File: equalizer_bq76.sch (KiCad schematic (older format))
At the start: 10 parts

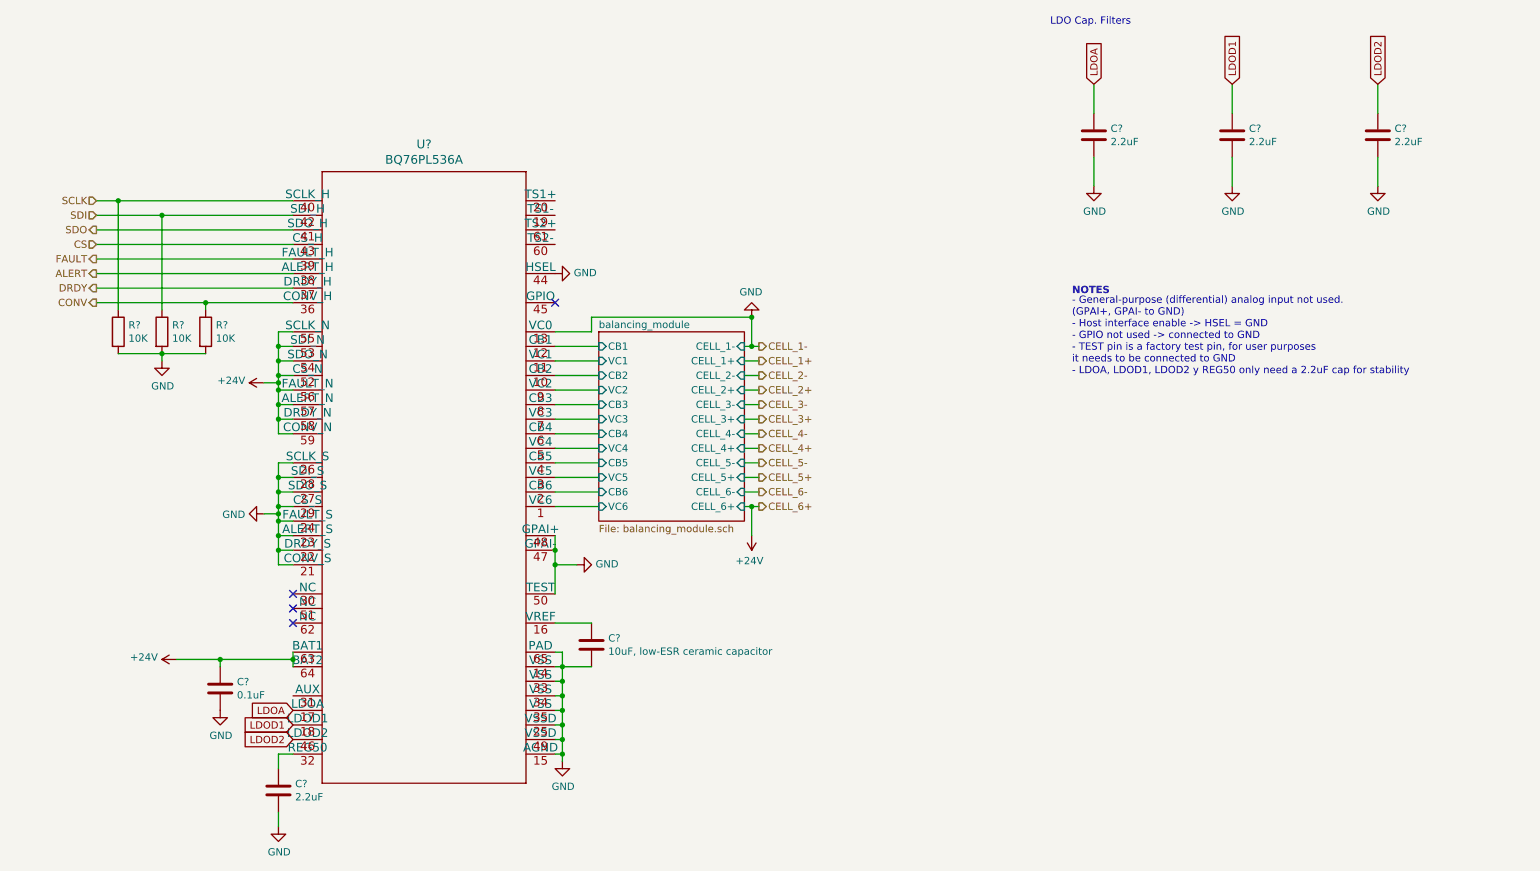
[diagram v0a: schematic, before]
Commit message: mmoya/bq76pl536a Adds current sensor and IO for hierarchical sheet
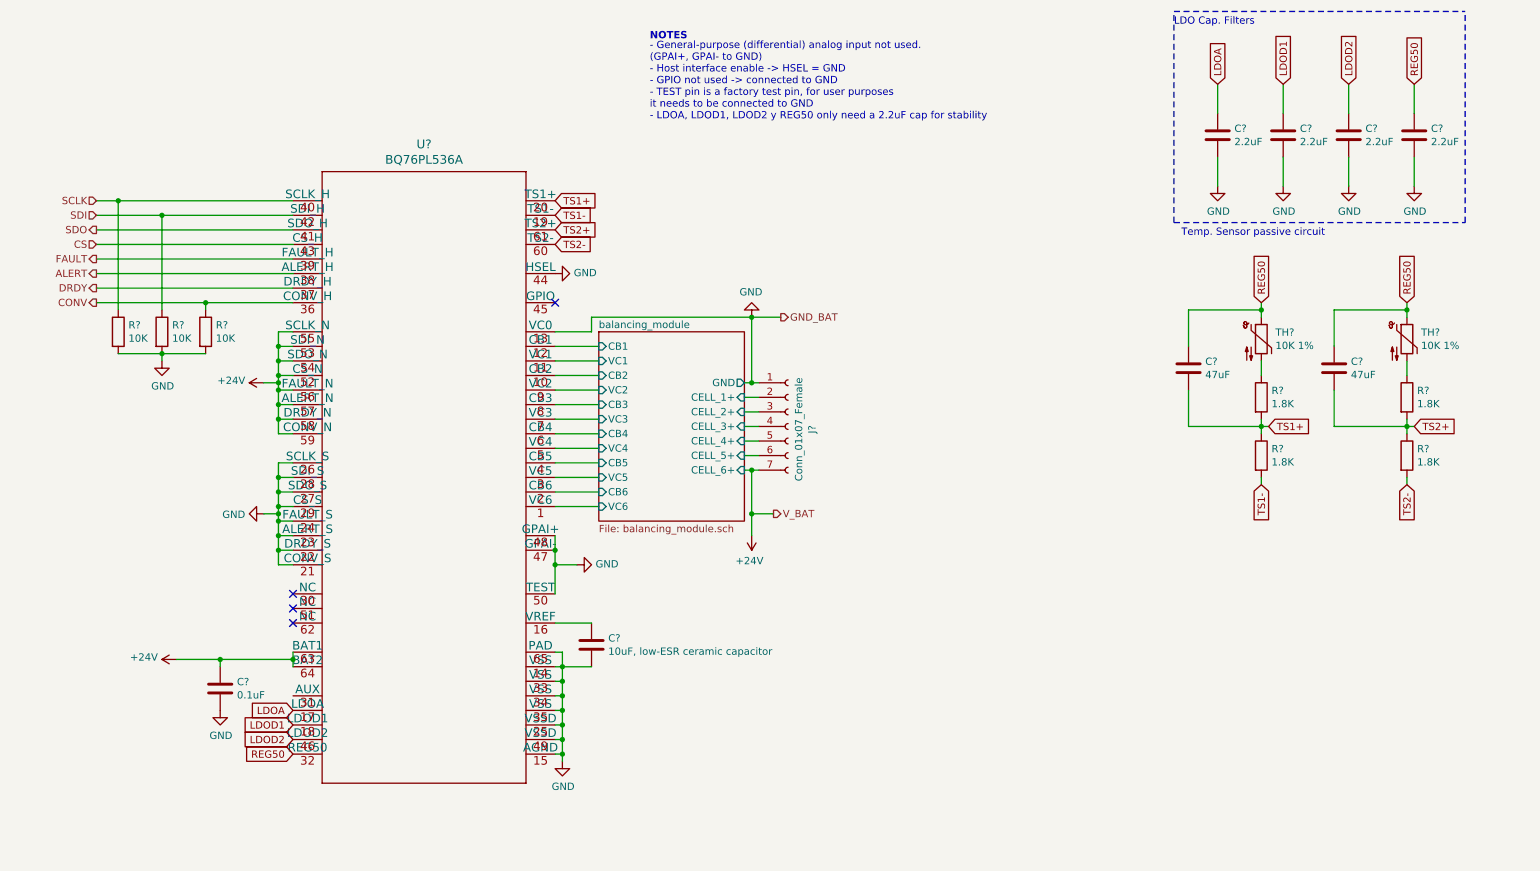
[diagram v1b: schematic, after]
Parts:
- removed C?: 2.2uF, Capacitor_SMD:C_0805_2012Metric_Pad1.18x1.45mm_HandSolder, symbol Device:C
- added C?: 2.2uF, Capacitor_SMD:C_0805_2012Metric_Pad1.18x1.45mm_HandSolder, symbol Device:C
- added C? (x2): 47uF, Capacitor_SMD:C_0805_2012Metric_Pad1.18x1.45mm_HandSolder, symbol Device:C
- added J?: Conn_01x07_Female, symbol Connector:Conn_01x07_Female
- added R? (x4): 1.8K, Resistor_SMD:R_0805_2012Metric_Pad1.20x1.40mm_HandSolder, symbol Device:R
- added TH? (x2): 10K 1%, Connector_JST:JST_XH_S2B-XH-A_1x02_P2.50mm_Horizontal, symbol Device:Thermistor_NTC
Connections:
- net +24V: now also J?.7 (Pin_7)
- net GND: now also C?.2, J?.1 (Pin_1)
- net TS1-: now reaches U?.19 (TS1-)
- net TS1-: now also R?.2
- net TS1+: now reaches U?.20 (TS1+)
- net TS1+: now also C?.2, R?.1, R?.2
- net REG50: now reaches U?.32 (REG50)
- net REG50: now also C?.1, C?.1, C?.1, TH?.1, TH?.1
- net TS2-: now reaches U?.60 (TS2-)
- net TS2-: now also R?.2
- net TS2+: now reaches U?.61 (TS2+)
- net TS2+: now also C?.2, R?.1, R?.2
- new net: R?.1, TH?.2 (x2)
- new net balancing_module/CELL_1+: J?.2 (Pin_2)
- new net balancing_module/CELL_2+: J?.3 (Pin_3)
- new net balancing_module/CELL_3+: J?.4 (Pin_4)
- new net balancing_module/CELL_4+: J?.5 (Pin_5)
- new net balancing_module/CELL_5+: J?.6 (Pin_6)
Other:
- note added: "Temp. Sensor passive circuit"
- moved on the sheet: C?

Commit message: Adds missing footprints for conns
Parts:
- J2: renamed from J?; footprint (none) -> Connector_JST:JST_XH_S7B-XH-A_1x07_P2.50mm_Horizontal
- gave numbers to parts that had none: 18
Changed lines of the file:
@@
 $EndDescr
 $Comp
-L power:GND #PWR?
+L power:GND #PWR0116
 U 1 1 5FE79F0F
 P 5000 5700
-F 0 "#PWR?" H 5000 5450 50  0001 C CNN
+F 0 "#PWR0116" H 5000 5450 50  0001 C CNN
 F 1 "GND" H 5005 5527 50  0000 C CNN
 F 2 "" H 5000 5700 50  0001 C CNN
@@
 	5000 5650 5000 5700
 $Comp
-L Device:C C?
+L Device:C C18
 U 1 1 5FE7B3CE
 P 5200 4900
-F 0 "C?" H 5315 4946 50  0000 L CNN
+F 0 "C18" H 5315 4946 50  0000 L CNN
 F 1 "10uF, low-ESR ceramic capacitor" H 5315 4855 50  0000 L CNN
 F 2 "Capacitor_SMD:C_0805_2012Metric_Pad1.18x1.45mm_HandSolder" H 5238 4750 50  0001 C CNN
@@
 	5200 2650 6300 2650
 $Comp
-L power:+24V #PWR?
+L power:+24V #PWR0117
 U 1 1 5FF5699F
 P 6300 4150
-F 0 "#PWR?" H 6300 4000 50  0001 C CNN
+F 0 "#PWR0117" H 6300 4000 50  0001 C CNN
 F 1 "+24V" H 6315 4323 50  0000 C CNN
 F 2 "" H 6300 4150 50  0001 C CNN
@@
 	3050 2850 3050 2950
 $Comp
-L power:+24V #PWR?
+L power:+24V #PWR0118
 U 1 1 5FF5DCD5
 P 2950 3100
-F 0 "#PWR?" H 2950 2950 50  0001 C CNN
+F 0 "#PWR0118" H 2950 2950 50  0001 C CNN
 F 1 "+24V" V 2965 3228 50  0000 L CNN
 F 2 "" H 2950 3100 50  0001 C CNN
@@
 	3150 5050 3150 5000
 $Comp
-L power:+24V #PWR?
+L power:+24V #PWR0119
 U 1 1 5FF6167E
 P 2350 5000
-F 0 "#PWR?" H 2350 4850 50  0001 C CNN
+F 0 "#PWR0119" H 2350 4850 50  0001 C CNN
 F 1 "+24V" V 2365 5128 50  0000 L CNN
 F 2 "" H 2350 5000 50  0001 C CNN
@@
 	3050 3750 3050 3850
 $Comp
-L power:GND #PWR?
+L power:GND #PWR0120
 U 1 1 5FF6D984
 P 2950 4000
-F 0 "#PWR?" H 2950 3750 50  0001 C CNN
+F 0 "#PWR0120" H 2950 3750 50  0001 C CNN
 F 1 "GND" V 2955 3872 50  0000 R CNN
 F 2 "" H 2950 4000 50  0001 C CNN
@@
 LDOD2
 $Comp
-L Device:C C?
+L Device:C C21
 U 1 1 5FF753CC
 P 9950 1400
-F 0 "C?" H 10065 1446 50  0000 L CNN
+F 0 "C21" H 10065 1446 50  0000 L CNN
 F 1 "2.2uF" H 10065 1355 50  0000 L CNN
 F 2 "Capacitor_SMD:C_0805_2012Metric_Pad1.18x1.45mm_HandSolder" H 9988 1250 50  0001 C CNN
@@
 $EndComp
 $Comp
-L power:GND #PWR?
+L power:GND #PWR0121
 U 1 1 5FF77895
 P 9950 1750
-F 0 "#PWR?" H 9950 1500 50  0001 C CNN
+F 0 "#PWR0121" H 9950 1500 50  0001 C CNN
 F 1 "GND" H 9955 1577 50  0000 C CNN
 F 2 "" H 9950 1750 50  0001 C CNN
@@
 LDOD2
 $Comp
-L Device:C C?
+L Device:C C23
 U 1 1 5FF9A6DD
 P 10400 1400
-F 0 "C?" H 10515 1446 50  0000 L CNN
+F 0 "C23" H 10515 1446 50  0000 L CNN
 F 1 "2.2uF" H 10515 1355 50  0000 L CNN
 F 2 "Capacitor_SMD:C_0805_2012Metric_Pad1.18x1.45mm_HandSolder" H 10438 1250 50  0001 C CNN
@@
 $EndComp
 $Comp
-L power:GND #PWR?
+L power:GND #PWR0122
 U 1 1 5FF9A6E5
 P 10400 1750
-F 0 "#PWR?" H 10400 1500 50  0001 C CNN
+F 0 "#PWR0122" H 10400 1500 50  0001 C CNN
 F 1 "GND" H 10405 1577 50  0000 C CNN
 F 2 "" H 10400 1750 50  0001 C CNN
@@
 $EndComp
 $Comp
-L Device:C C?
+L Device:C C20
 U 1 1 5FFA673C
 P 9500 1400
-F 0 "C?" H 9615 1446 50  0000 L CNN
+F 0 "C20" H 9615 1446 50  0000 L CNN
 F 1 "2.2uF" H 9615 1355 50  0000 L CNN
 F 2 "Capacitor_SMD:C_0805_2012Metric_Pad1.18x1.45mm_HandSolder" H 9538 1250 50  0001 C CNN
@@
 $EndComp
 $Comp
-L power:GND #PWR?
+L power:GND #PWR0123
 U 1 1 5FFA6744
 P 9500 1750
-F 0 "#PWR?" H 9500 1500 50  0001 C CNN
+F 0 "#PWR0123" H 9500 1500 50  0001 C CNN
 F 1 "GND" H 9505 1577 50  0000 C CNN
 F 2 "" H 9500 1750 50  0001 C CNN
@@
 $EndComp
 $Comp
-L Device:C C?
+L Device:C C17
 U 1 1 5FFAD9BF
 P 2650 5200
-F 0 "C?" H 2765 5246 50  0000 L CNN
+F 0 "C17" H 2765 5246 50  0000 L CNN
 F 1 "0.1uF" H 2765 5155 50  0000 L CNN
 F 2 "Capacitor_SMD:C_0805_2012Metric_Pad1.18x1.45mm_HandSolder" H 2688 5050 50  0001 C CNN
@@
 	2650 5000 3150 5000
 $Comp
-L power:GND #PWR?
+L power:GND #PWR0124
 U 1 1 5FFB4473
 P 2650 5350
-F 0 "#PWR?" H 2650 5100 50  0001 C CNN
+F 0 "#PWR0124" H 2650 5100 50  0001 C CNN
 F 1 "GND" H 2655 5177 50  0000 C CNN
 F 2 "" H 2650 5350 50  0001 C CNN
@@
 $EndComp
 $Comp
-L power:GND #PWR?
+L power:GND #PWR0125
 U 1 1 5FFB8D43
 P 4950 2350
-F 0 "#PWR?" H 4950 2100 50  0001 C CNN
+F 0 "#PWR0125" H 4950 2100 50  0001 C CNN
 F 1 "GND" V 4955 2222 50  0000 R CNN
 F 2 "" H 4950 2350 50  0001 C CNN
@@
 LDO Cap. Filters
 $Comp
-L power:GND #PWR?
+L power:GND #PWR0126
 U 1 1 6001D855
 P 5100 4350
-F 0 "#PWR?" H 5100 4100 50  0001 C CNN
+F 0 "#PWR0126" H 5100 4100 50  0001 C CNN
 F 1 "GND" V 5105 4222 50  0000 R CNN
 F 2 "" H 5100 4350 50  0001 C CNN
@@
 LDOA
 $Comp
-L Device:R R?
+L Device:R R4
 U 1 1 6003EECE
 P 1950 2750
-F 0 "R?" H 2020 2796 50  0000 L CNN
+F 0 "R4" H 2020 2796 50  0000 L CNN
 F 1 "10K" H 2020 2705 50  0000 L CNN
 F 2 "Resistor_SMD:R_0805_2012Metric_Pad1.20x1.40mm_HandSolder" V 1880 2750 50  0001 C CNN
@@
 $EndComp
 $Comp
-L Device:R R?
+L Device:R R5
 U 1 1 6003F38A
 P 2250 2750
-F 0 "R?" H 2320 2796 50  0000 L CNN
+F 0 "R5" H 2320 2796 50  0000 L CNN
 F 1 "10K" H 2320 2705 50  0000 L CNN
 F 2 "Resistor_SMD:R_0805_2012Metric_Pad1.20x1.40mm_HandSolder" V 2180 2750 50  0001 C CNN
@@
 $EndComp
 $Comp
-L Device:R R?
+L Device:R R6
 U 1 1 6003F59D
 P 2550 2750
-F 0 "R?" H 2620 2796 50  0000 L CNN
+F 0 "R6" H 2620 2796 50  0000 L CNN
 F 1 "10K" H 2620 2705 50  0000 L CNN
 F 2 "Resistor_SMD:R_0805_2012Metric_Pad1.20x1.40mm_HandSolder" V 2480 2750 50  0001 C CNN
@@
 	2250 2900 2550 2900
 $Comp
-L power:GND #PWR?
+L power:GND #PWR0127
 U 1 1 6005D886
 P 2250 2950
-F 0 "#PWR?" H 2250 2700 50  0001 C CNN
+F 0 "#PWR0127" H 2250 2700 50  0001 C CNN
 F 1 "GND" H 2255 2777 50  0000 C CNN
 F 2 "" H 2250 2950 50  0001 C CNN
@@
 Connection ~ 2550 2550
 $Comp
-L power:GND #PWR?
+L power:GND #PWR0128
 U 1 1 5FEA2AD8
 P 6300 2650
-F 0 "#PWR?" H 6300 2400 50  0001 C CNN
+F 0 "#PWR0128" H 6300 2400 50  0001 C CNN
 F 1 "GND" H 6305 2477 50  0000 C CNN
 F 2 "" H 6300 2650 50  0001 C CNN
@@
 $EndComp
 $Comp
-L Device:R R?
+L Device:R R9
 U 1 1 5FE93DA5
 P 10800 3200
-F 0 "R?" H 10870 3246 50  0000 L CNN
+F 0 "R9" H 10870 3246 50  0000 L CNN
 F 1 "1.8K" H 10870 3155 50  0000 L CNN
 F 2 "Resistor_SMD:R_0805_2012Metric_Pad1.20x1.40mm_HandSolder" V 10730 3200 50  0001 C CNN
@@
 $EndComp
 $Comp
-L Device:R R?
+L Device:R R10
 U 1 1 5FE942F6
 P 10800 3600
-F 0 "R?" H 10870 3646 50  0000 L CNN
+F 0 "R10" H 10870 3646 50  0000 L CNN
 F 1 "1.8K" H 10870 3555 50  0000 L CNN
 F 2 "Resistor_SMD:R_0805_2012Metric_Pad1.20x1.40mm_HandSolder" V 10730 3600 50  0001 C CNN
@@
 Temp. Sensor passive circuit
 $Comp
-L Device:Thermistor_NTC TH?
+L Device:Thermistor_NTC TH2
 U 1 1 5FEB224A
 P 10800 2800
-F 0 "TH?" H 10897 2846 50  0000 L CNN
+F 0 "TH2" H 10897 2846 50  0000 L CNN
 F 1 "10K 1%" H 10897 2755 50  0000 L CNN
 F 2 "Connector_JST:JST_XH_S2B-XH-A_1x02_P2.50mm_Horizontal" H 10800 2850 50  0001 C CNN
@@
 Connection ~ 4950 4250
 $Comp
-L Battery_Management:BQ76PL536A U?
+L Battery_Management:BQ76PL536A U2
 U 1 1 5FE7709D
 P 4050 3750
-F 0 "U?" H 4050 6038 60  0000 C CNN
+F 0 "U2" H 4050 6038 60  0000 C CNN
 F 1 "BQ76PL536A" H 4050 5932 60  0000 C CNN
 F 2 "Package_QFP:HTQFP-64-1EP_10x10mm_P0.5mm_EP8x8mm" H 4050 3690 60  0001 C CNN
@@
 REG50
 $Comp
-L Device:C C?
+L Device:C C24
 U 1 1 5FECF8E1
 P 10850 1400
-F 0 "C?" H 10965 1446 50  0000 L CNN
+F 0 "C24" H 10965 1446 50  0000 L CNN
 F 1 "2.2uF" H 10965 1355 50  0000 L CNN
 F 2 "Capacitor_SMD:C_0805_2012Metric_Pad1.18x1.45mm_HandSolder" H 10888 1250 50  0001 C CNN
@@
 $EndComp
 $Comp
-L power:GND #PWR?
+L power:GND #PWR0129
 U 1 1 5FECF8E7
 P 10850 1750
-F 0 "#PWR?" H 10850 1500 50  0001 C CNN
+F 0 "#PWR0129" H 10850 1500 50  0001 C CNN
 F 1 "GND" H 10855 1577 50  0000 C CNN
 F 2 "" H 10850 1750 50  0001 C CNN
@@
 REG50
 $Comp
-L Device:C C?
+L Device:C C22
 U 1 1 5FEFD46C
 P 10300 3000
-F 0 "C?" H 10415 3046 50  0000 L CNN
+F 0 "C22" H 10415 3046 50  0000 L CNN
 F 1 "47uF" H 10415 2955 50  0000 L CNN
 F 2 "Capacitor_SMD:C_0805_2012Metric_Pad1.18x1.45mm_HandSolder" H 10338 2850 50  0001 C CNN
@@
 	10800 3750 10800 3800
 $Comp
-L Device:R R?
+L Device:R R7
 U 1 1 5FF2491E
 P 9800 3200
-F 0 "R?" H 9870 3246 50  0000 L CNN
+F 0 "R7" H 9870 3246 50  0000 L CNN
 F 1 "1.8K" H 9870 3155 50  0000 L CNN
 F 2 "Resistor_SMD:R_0805_2012Metric_Pad1.20x1.40mm_HandSolder" V 9730 3200 50  0001 C CNN
@@
 $EndComp
 $Comp
-L Device:R R?
+L Device:R R8
 U 1 1 5FF24924
 P 9800 3600
-F 0 "R?" H 9870 3646 50  0000 L CNN
+F 0 "R8" H 9870 3646 50  0000 L CNN
 F 1 "1.8K" H 9870 3555 50  0000 L CNN
 F 2 "Resistor_SMD:R_0805_2012Metric_Pad1.20x1.40mm_HandSolder" V 9730 3600 50  0001 C CNN
@@
 	9800 3350 9800 3400
 $Comp
-L Device:Thermistor_NTC TH?
+L Device:Thermistor_NTC TH1
 U 1 1 5FF2492B
 P 9800 2800
-F 0 "TH?" H 9897 2846 50  0000 L CNN
+F 0 "TH1" H 9897 2846 50  0000 L CNN
 F 1 "10K 1%" H 9897 2755 50  0000 L CNN
 F 2 "Connector_JST:JST_XH_S2B-XH-A_1x02_P2.50mm_Horizontal" H 9800 2850 50  0001 C CNN
@@
 REG50
 $Comp
-L Device:C C?
+L Device:C C19
 U 1 1 5FF24933
 P 9300 3000
-F 0 "C?" H 9415 3046 50  0000 L CNN
+F 0 "C19" H 9415 3046 50  0000 L CNN
 F 1 "47uF" H 9415 2955 50  0000 L CNN
 F 2 "Capacitor_SMD:C_0805_2012Metric_Pad1.18x1.45mm_HandSolder" H 9338 2850 50  0001 C CNN
@@
 Connection ~ 6300 2650
 $Comp
-L Connector:Conn_01x07_Female J?
+L Connector:Conn_01x07_Female J2
 U 1 1 5FF8226F
 P 6550 3400
-F 0 "J?" V 6715 3380 50  0000 C CNN
+F 0 "J2" V 6715 3380 50  0000 C CNN
 F 1 "Conn_01x07_Female" V 6624 3380 50  0000 C CNN
-F 2 "" H 6550 3400 50  0001 C CNN
+F 2 "Connector_JST:JST_XH_S7B-XH-A_1x07_P2.50mm_Horizontal" H 6550 3400 50  0001 C CNN
 F 3 "~" H 6550 3400 50  0001 C CNN
 	1    6550 3400

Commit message: Changes overlapping names of pins between bq76 and ina226
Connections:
- net ALERT renamed ALERT_BQ76
- net CONV renamed CONV_BQ76
- net DRDY renamed DRDY_BQ76
- net FAULT renamed FAULT_BQ76
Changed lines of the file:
@@
 $Descr A4 11693 8268
 encoding utf-8
-Sheet 3 5
+Sheet 2 5
 Title ""
 Date ""
@@
 	3150 2150 1800 2150
 Text HLabel 1800 2250 0    50   Output ~ 0
-FAULT
+FAULT_BQ76
 Wire Wire Line
 	1800 2250 3150 2250
 Text HLabel 1800 2350 0    50   Output ~ 0
-ALERT
+ALERT_BQ76
 Wire Wire Line
 	1800 2350 3150 2350
 Text HLabel 1800 2450 0    50   Output ~ 0
-DRDY
+DRDY_BQ76
 Wire Wire Line
 	3150 2450 1800 2450
 Text HLabel 1800 2550 0    50   Output ~ 0
-CONV
+CONV_BQ76
 Wire Wire Line
 	2550 2550 1800 2550

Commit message: Added bat_charger.sch to main hierarchical bms project
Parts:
- U2: symbol Battery_Management:BQ76PL536A -> bms_hardware-rescue:BQ76PL536A-Battery_Management
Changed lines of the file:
@@
 $Descr A4 11693 8268
 encoding utf-8
-Sheet 2 5
+Sheet 4 6
 Title ""
 Date ""
@@
 Connection ~ 4950 4250
 $Comp
-L Battery_Management:BQ76PL536A U2
+L bms_hardware-rescue:BQ76PL536A-Battery_Management U2
 U 1 1 5FE7709D
 P 4050 3750
+AR Path="/5FE7709D" Ref="U2"  Part="1"
+AR Path="/5FE7678E/5FE7709D" Ref="U2"  Part="1"
 F 0 "U2" H 4050 6038 60  0000 C CNN
 F 1 "BQ76PL536A" H 4050 5932 60  0000 C CNN
